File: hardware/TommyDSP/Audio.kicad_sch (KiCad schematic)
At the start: 34 parts, among them U301 ES8388

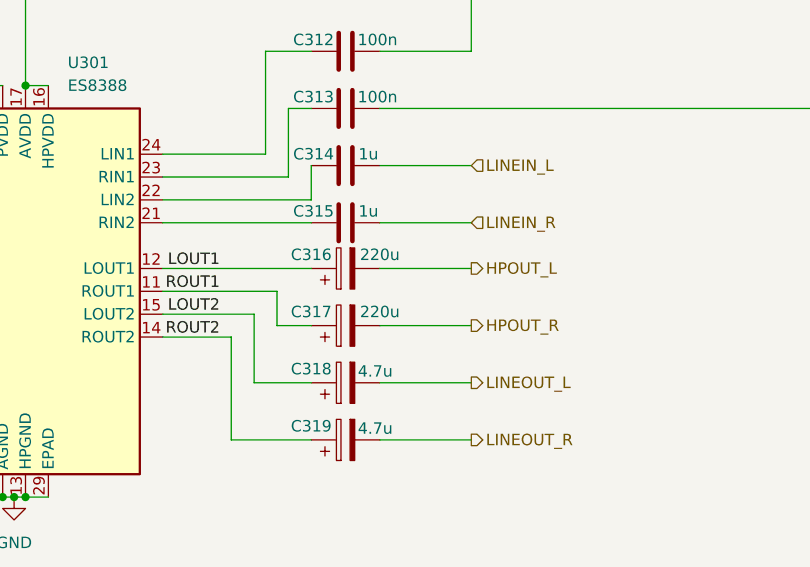
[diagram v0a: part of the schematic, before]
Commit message: hardware: adjust value of BUCK feedback resistors
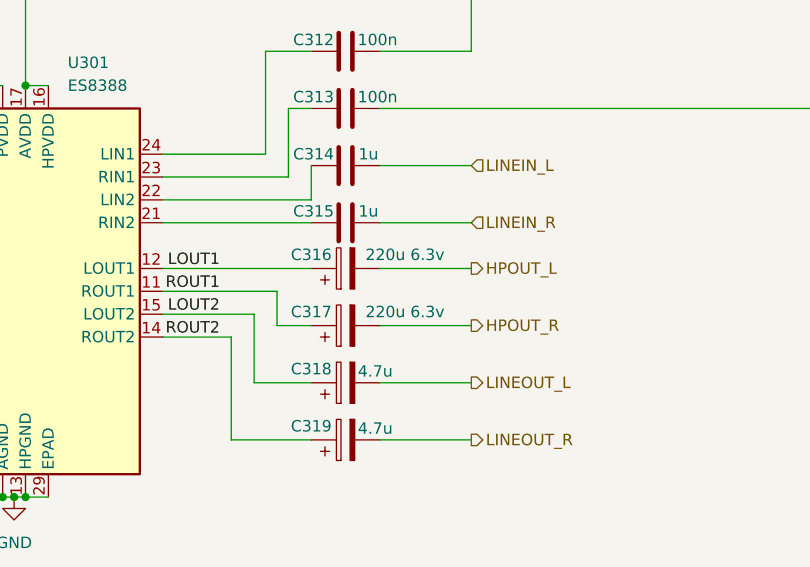
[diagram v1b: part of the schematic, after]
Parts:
- C316, C317: value 220u -> 220u 6.3v
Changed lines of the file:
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@@
 			)
 		)
-		(property "Value" "220u"
-			(at 165.1 107.696 90)
+		(property "Value" "220u 6.3v"
+			(at 167.894 107.696 90)
 			(effects
 				(font
@@
 			)
 		)
-		(property "Value" "220u"
-			(at 165.1 114.046 90)
-			(effects
-				(font
+		(property "Value" "220u 6.3v"
+			(at 167.894 114.046 90)
+			(effects
+				(font

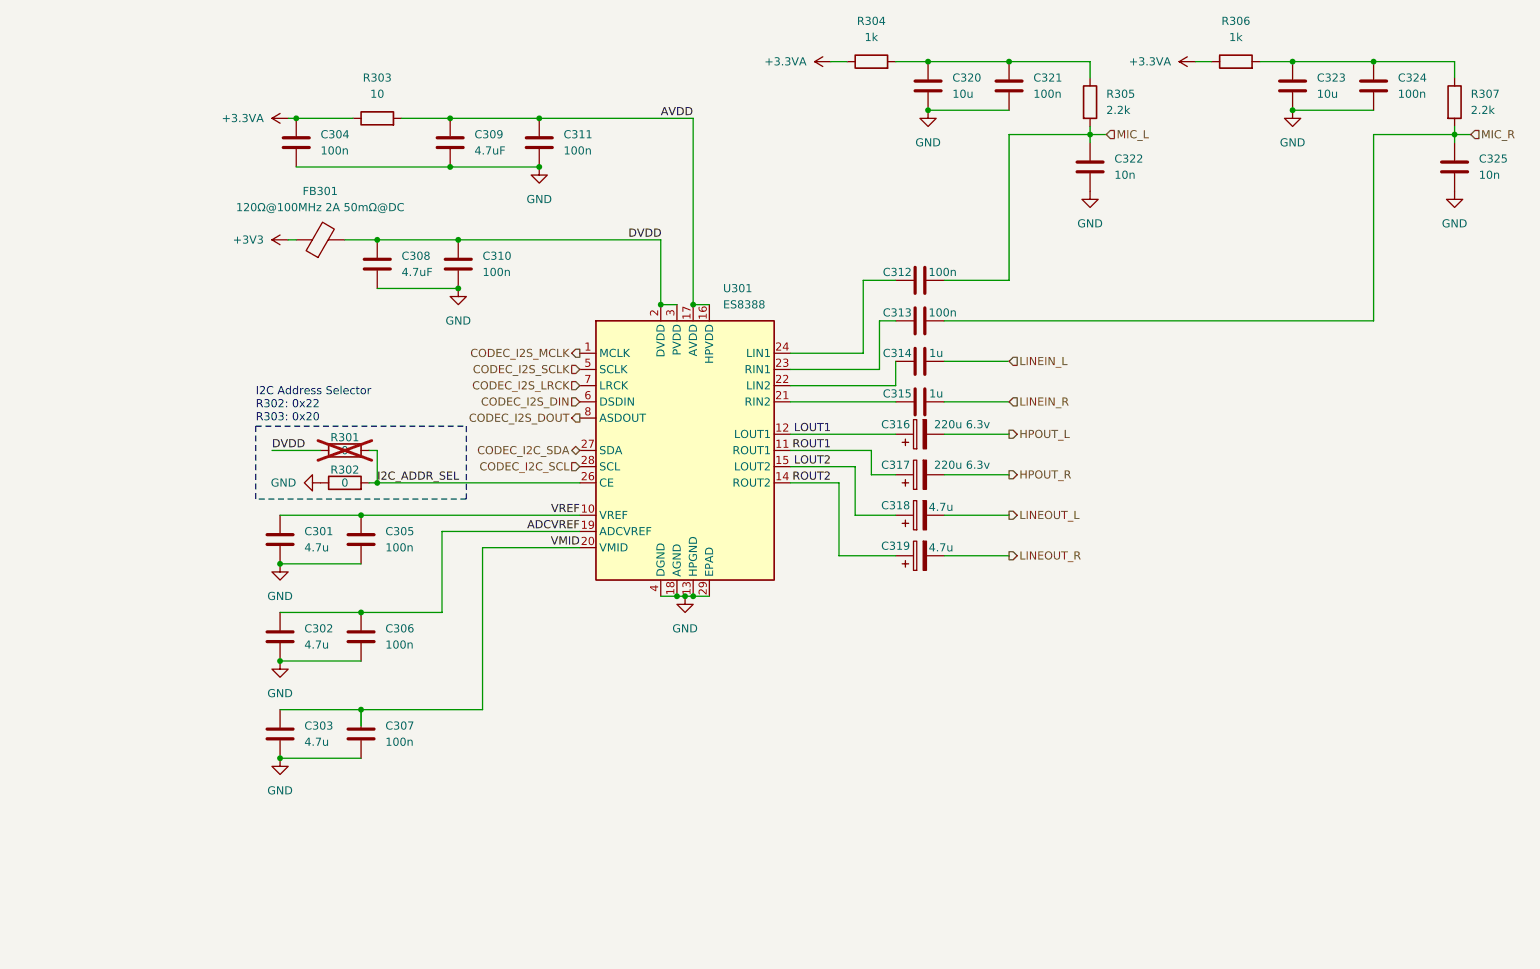
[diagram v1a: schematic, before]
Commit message: hardware: add compatibility for WM8988 CODEC
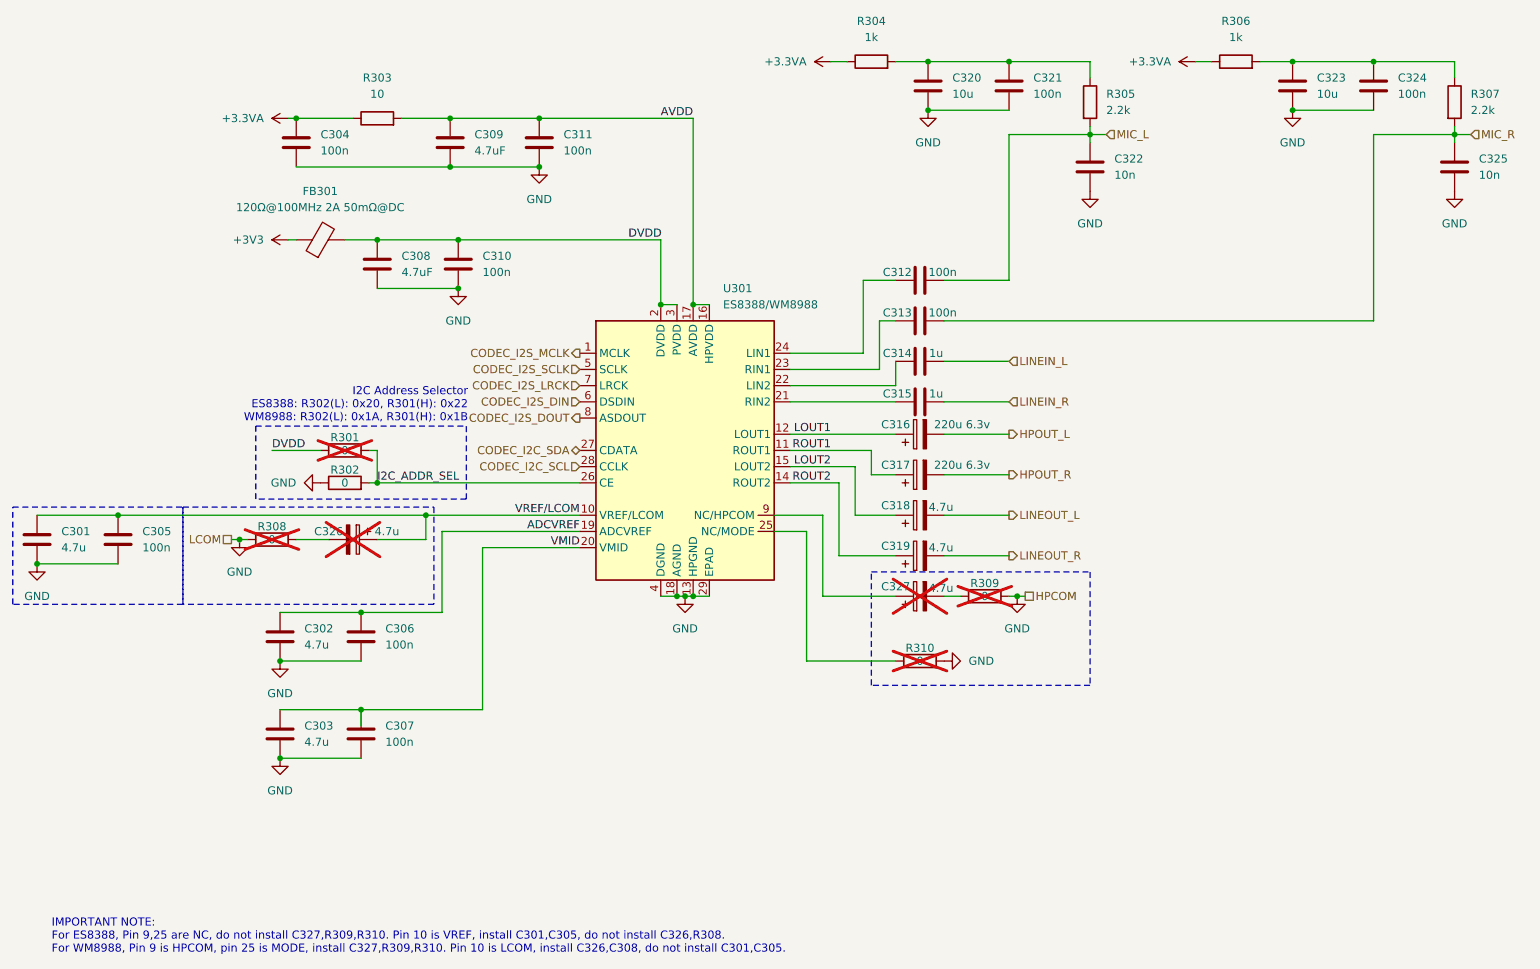
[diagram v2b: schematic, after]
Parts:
- removed U301: ES8388, Package_DFN_QFN:QFN-28-1EP_4x4mm_P0.45mm_EP2.6x2.6mm, symbol Audio:ES8388
- added C326, C327: 4.7u, Capacitor_THT:CP_Radial_D5.0mm_P2.50mm, symbol Device:C_Polarized
- added R308, R309, R310: 0, Resistor_SMD:R_0603_1608Metric, symbol Device:R
- added U301: ES8388/WM8988, Package_DFN_QFN:QFN-28-1EP_4x4mm_P0.45mm_EP2.6x2.6mm, symbol Project:ES8388/WM8988
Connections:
- net ADCVREF: now also U301.19 (ADCVREF)
- net AVDD: now also U301.16 (HPVDD), U301.17 (AVDD)
- net CODEC_I2C_SCL: now also U301.28 (CCLK)
- net CODEC_I2C_SDA: now also U301.27 (CDATA)
- net CODEC_I2S_DIN: now also U301.6 (DSDIN)
- net CODEC_I2S_DOUT: now also U301.8 (ASDOUT)
- net CODEC_I2S_LRCK: now also U301.7 (LRCK)
- net CODEC_I2S_MCLK: now also U301.1 (MCLK)
- net CODEC_I2S_SCLK: now also U301.5 (SCLK)
- net DVDD: now also U301.2 (DVDD), U301.3 (PVDD)
- net GND: now also R308.1, R309.2, R310.2, U301.13 (HPGND), U301.18 (AGND), U301.29 (EPAD), U301.4 (DGND)
- net I2C_ADDR_SEL: now also U301.26 (CE)
- net LOUT1: now also U301.12 (LOUT1)
- net LOUT2: now also U301.15 (LOUT2)
- net ROUT1: now also U301.11 (ROUT1)
- net ROUT2: now also U301.14 (ROUT2)
- net VMID: now also U301.20 (VMID)
- net at C313.1: now also U301.23 (RIN1)
- net at C312.1: now also U301.24 (LIN1)
- net at C314.1: now also U301.22 (LIN2)
- net at C315.1: now also U301.21 (RIN2)
- net VREF renamed VREF/LCOM
- net VREF/LCOM: now also C326.1, U301.10 (VREF/LCOM)
- new net: C327.1, U301.9 (NC/HPCOM)
- new net: C327.2, R309.1
- new net: R310.1, U301.25 (NC/MODE)
- new net: C326.2, R308.2
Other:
- note added: "I2C Address Selector ES8388: R302(L): 0x20, R301(H): 0x22 WM8988: R302(L): 0x1A, R301(H): 0x1B"
- note added: "IMPORTANT NOTE: For ES8388, Pin 9,25 are NC, do not install C327,R309,R310. Pin 10 is VREF, install C301,C305, do not install C326,R308. For WM8988, Pin 9 is HPCOM, pin 25 is MODE, install C327,R309,R310. Pin 10 is LCOM, install C326,C308, do not install C301,C305."
- note removed: "I2C Address Selector R302: 0x22 R303: 0x20"
- moved on the sheet: C301, C305
